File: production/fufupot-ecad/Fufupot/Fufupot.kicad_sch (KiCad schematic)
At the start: 56 parts, among them IC1 FOD3150, J1 Conn_01x04_Pin, J1 USB_B, J10 Conn_01x03, J3 Conn_01x03, J4 Conn_01x02_Pin, J5 Conn_01x02_Pin, J6 Conn_01x03_Pin, J7 Conn_01x02_Pin, J9 Conn_01x04_Pin, SW1 SW_Push, U1 STGP8NC60KD, U2 FT232RL, U2 LM5165DRC, U3 USBLC6-2SC6, U4 ATMEGA328P-PN

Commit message: Update Fufupot.kicad_sch
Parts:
- removed J1, J9: Conn_01x04_Pin, symbol Connector:Conn_01x04_Pin
- removed J4, J5, J7: Conn_01x02_Pin, symbol Connector:Conn_01x02_Pin
- removed J6: Conn_01x03_Pin, symbol Connector:Conn_01x03_Pin
- added J1, J8: Conn_01x04, symbol Connector_Generic:Conn_01x04
- added J11: Conn_01x03, symbol Connector_Generic:Conn_01x03
- added J5, J6, J7: Conn_01x02, symbol Connector_Generic:Conn_01x02
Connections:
- net +48V: now also J10.3 (Pin_3)
- net +5V: now also J10.2 (Pin_2), J11.2 (Pin_2)
- net A4: now also J5.2 (Pin_2)
- net A5: now also J5.1 (Pin_1)
- net D_Buzz: now also J6.1 (Pin_1)
- net D_Red: now also J8.3 (Pin_3)
- net D_Switch: now also J8.2 (Pin_2)
- net GND: now also J10.1 (Pin_1), J11.3 (Pin_3), J6.2 (Pin_2), J7.2 (Pin_2), J8.1 (Pin_1), J8.4 (Pin_4); no longer U2.18 (GND), U2.21 (GND), U2.7 (GND)
- net MISO: now also J1.3 (Pin_3)
- net MOSI: now also J1.2 (Pin_2)
- net SCK: now also J1.4 (Pin_4)
- net SS: now also J1.1 (Pin_1)
- net at R2.2: now also J11.1 (Pin_1)
- net at R2.2: now also J7.1 (Pin_1)
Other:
- moved on the sheet: C1, C3, C4, C5, IC1, J3, L1, L2, R1, R19, R2, R3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

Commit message: Kicad updates yay
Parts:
- removed 102PS1J1, 102PS1J2: 1k, symbol Device:R
- removed L1: L, symbol Device:L
- added J12, J4, J9: Conn_01x02, B2B-XH-A_LF__SN_:JST_B2B-XH-A_LF__SN_, symbol Connector_Generic:Conn_01x02
- C3: footprint (none) -> U1-E_NCH; symbol Device:C_Polarized -> 2023-11-09_20-43-14:UVZ1E100MDD
- C4: footprint (none) -> 8600footprint:CAP_WCAP-ATG5_05.0X11.0_WRE; symbol Device:C_Polarized -> 2023-11-09_20-51-41:860020772001
- C5: footprint (none) -> ECWfootprints:CAP_ECWFL_STRAIGHT_20.5LX11.9TX18.5H_PAN; symbol Device:C_Polarized -> 2023-11-09_20-58-51:ECW-F6364JL
- IC1: footprint DIP762W56P254L966H508Q8N -> FODfootprints:SMD8_9P91X6P86_ONS
- J1, J8: footprint (none) -> 4PINfootprints:CONN_B4B-XH-A_JST
- J10, J11, J3: footprint (none) -> 3PINfootprints:CONN_B3B-ZR_JST
- J5, J6, J7: footprint (none) -> B2B-XH-A_LF__SN_:JST_B2B-XH-A_LF__SN_
- L2: footprint (none) -> INDPM:INDPM176169X700N; symbol Device:L -> SRP1770CC-100M:SRP1770CC-100M; Height (none) -> 7; Manufacturer_Name (none) -> Bourns; Manufacturer_Part_Number (none) -> SRP1770CC-100M
- R1: footprint (none) -> SQPfootprints:RES_SQP500_22X9P5_YAG; symbol Device:R -> 2023-11-09_21-42-51:SQP500JB-0R91
- R12, R13, R19, R2, R20, R3, R4, R5, R7: footprint (none) -> Resistor_SMD:R_0805_2012Metric
- R2: value 220 -> 200; footprint (none) -> Resistor_SMD:R_0805_2012Metric
- U1: footprint TO-220FP_STM -> TO225P1040X460X1968-3(1):TO225P1040X460X1968-3
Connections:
- net +5V: now also J12.2 (Pin_2), J9.2 (Pin_2)
- net A2: now also J9.1 (Pin_1)
- net A3: now also J12.1 (Pin_1)
- net GND: now also C1.2
- net at C5.2, U1.2 (C): now also J4.1 (Pin_1)
- net at C1.1, C5.1, L2.2: now also J4.2 (Pin_2)

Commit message: Fixed switches
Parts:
- 16MHz1: footprint 16 MHz Xtal Osc:XTAL_ABL-16_ABR -> crystalfootprints:XTAL_ABL-16_ABR
- C5, C6: footprint 22 pF Cap:CAP_K-SERIES_15-L2_VIS -> 22pFfootprints:CAP_K-SERIES_15-L2_VIS
- C7: footprint 10 uF Cap:CAP_YX_5X11_RUB -> 10uFfootprints:CAP_YX_5X11_RUB
- C8: footprint (none) -> 0.1uFfootprints:CAP_Y5VE5TL2_VIS
- SW1: footprint (none) -> TS02-66-50-BK-100-SCR-D:SW_TS02-66-50-BK-100-SCR-D
- SW1: footprint Button_Switch_SMD:SW_DIP_SPSTx04_Slide_6.7x11.72mm_W6.73mm_P2.54mm_LowProfile_JPin -> TS02-66-50-BK-100-SCR-D:SW_TS02-66-50-BK-100-SCR-D
- U4: footprint footprints:28P3_ATM -> ATmegafootprints:28P3_ATM
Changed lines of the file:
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@@
       (effects (font (size 1.27 1.27)) (justify left))
     )
-    (property "Footprint" "22 pF Cap:CAP_K-SERIES_15-L2_VIS" (at 281.94 235.2548 0)
+    (property "Footprint" "22pFfootprints:CAP_K-SERIES_15-L2_VIS" (at 281.94 235.2548 0)
       (effects (font (size 1.27 1.27)) hide)
     )
@@
       (effects (font (size 1.27 1.27)))
     )
-    (property "Footprint" "" (at 172.72 115.57 0)
+    (property "Footprint" "TS02-66-50-BK-100-SCR-D:SW_TS02-66-50-BK-100-SCR-D" (at 172.72 115.57 0)
       (effects (font (size 1.27 1.27)) hide)
     )
@@
       (effects (font (size 1.27 1.27)) (justify left))
     )
-    (property "Footprint" "22 pF Cap:CAP_K-SERIES_15-L2_VIS" (at 281.94 221.2848 0)
+    (property "Footprint" "22pFfootprints:CAP_K-SERIES_15-L2_VIS" (at 281.94 221.2848 0)
       (effects (font (size 1.27 1.27)) hide)
     )
@@
       (effects (font (size 1.27 1.27)) (justify left))
     )
-    (property "Footprint" "" (at 289.2552 205.74 0)
+    (property "Footprint" "0.1uFfootprints:CAP_Y5VE5TL2_VIS" (at 289.2552 205.74 0)
       (effects (font (size 1.27 1.27)) hide)
     )
@@
       (effects (font (size 1.524 1.524)))
     )
-    (property "Footprint" "footprints:28P3_ATM" (at 288.29 199.39 0)
+    (property "Footprint" "ATmegafootprints:28P3_ATM" (at 288.29 199.39 0)
       (effects (font (size 1.27 1.27) italic) hide)
     )
@@
       (effects (font (size 1.27 1.27)))
     )
-    (property "Footprint" "Button_Switch_SMD:SW_DIP_SPSTx04_Slide_6.7x11.72mm_W6.73mm_P2.54mm_LowProfile_JPin" (at 194.31 262.89 0)
+    (property "Footprint" "TS02-66-50-BK-100-SCR-D:SW_TS02-66-50-BK-100-SCR-D" (at 194.31 262.89 0)
       (effects (font (size 1.27 1.27)) hide)
     )
@@
       (effects (font (size 1.27 1.27)) (justify right))
     )
-    (property "Footprint" "16 MHz Xtal Osc:XTAL_ABL-16_ABR" (at 287.02 228.6 0)
+    (property "Footprint" "crystalfootprints:XTAL_ABL-16_ABR" (at 287.02 228.6 0)
       (effects (font (size 1.27 1.27)) hide)
     )
@@
       (effects (font (size 1.27 1.27)) (justify left))
     )
-    (property "Footprint" "10 uF Cap:CAP_YX_5X11_RUB" (at 282.9052 205.74 0)
-      (effects (font (size 1.27 1.27)) hide)
-    )
+    (property "Footprint" "10uFfootprints:CAP_YX_5X11_RUB" (at 282.9052 205.74 0)
+      (effects (font (size 1.27 1.27)) hide)
+    )

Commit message: Updating USB
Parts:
- J1: footprint Connector_USB:USB_Micro-B_Amphenol_10104110_Horizontal -> UJ2-BH-W1-TH:CUI_UJ2-BH-W1-TH
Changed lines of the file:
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@@
       (effects (font (size 1.27 1.27)))
     )
-    (property "Footprint" "Connector_USB:USB_Micro-B_Amphenol_10104110_Horizontal" (at 31.75 114.3 0)
+    (property "Footprint" "UJ2-BH-W1-TH:CUI_UJ2-BH-W1-TH" (at 31.75 114.3 0)
       (effects (font (size 1.27 1.27)) hide)
     )

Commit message: pcb layout
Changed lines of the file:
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@@
   (junction (at 322.58 113.03) (diameter 0) (color 0 0 0 0)
   )
-  (junction (at 175.26 241.3) (diameter 0) (color 0 0 0 0)
-  )
   (junction (at 370.84 57.15) (diameter 0) (color 0 0 0 0)
   )
@@
   )
   (junction (at 271.78 46.99) (diameter 0) (color 0 0 0 0)
-  )
-  (junction (at 175.26 238.76) (diameter 0) (color 0 0 0 0)
-  )
-  (junction (at 175.26 245.11) (diameter 0) (color 0 0 0 0)
   )
   (junction (at 49.53 48.26) (diameter 0) (color 0 0 0 0)
@@
     (stroke (width 0) (type default))
   )
-  (wire (pts (xy 175.26 238.76) (xy 184.15 238.76))
-    (stroke (width 0) (type default))
-  )
   (wire (pts (xy 26.67 191.77) (xy 35.56 191.77))
     (stroke (width 0) (type default))
@@
     (stroke (width 0) (type default))
   )
-  (wire (pts (xy 175.26 236.22) (xy 175.26 238.76))
-    (stroke (width 0) (type default))
-  )
   (wire (pts (xy 364.49 76.2) (xy 361.95 76.2))
     (stroke (width 0) (type default))
@@
     (stroke (width 0) (type default))
   )
-  (wire (pts (xy 184.15 236.22) (xy 175.26 236.22))
+  (wire (pts (xy 176.53 236.22) (xy 176.53 237.49))
     (stroke (width 0) (type default))
   )
@@
     (stroke (width 0) (type default))
   )
-  (wire (pts (xy 175.26 241.3) (xy 184.15 241.3))
-    (stroke (width 0) (type default))
-  )
   (wire (pts (xy 341.63 62.23) (xy 344.17 62.23))
     (stroke (width 0) (type default))
@@
     (stroke (width 0) (type default))
   )
-  (wire (pts (xy 175.26 241.3) (xy 175.26 245.11))
-    (stroke (width 0) (type default))
-  )
   (wire (pts (xy 322.58 113.03) (xy 323.85 113.03))
     (stroke (width 0) (type default))
@@
   )
   (wire (pts (xy 360.68 237.49) (xy 367.03 237.49))
-    (stroke (width 0) (type default))
-  )
-  (wire (pts (xy 175.26 238.76) (xy 175.26 241.3))
     (stroke (width 0) (type default))
   )
@@
         )
       )
+    )
+  )
+  (symbol (lib_id "power:GND") (at 176.53 237.49 0) (unit 1)
+    (in_bom yes) (on_board yes) (dnp no) (fields_autoplaced)
+    (property "Reference" "#PWR047" (at 176.53 243.84 0)
+      (effects (font (size 1.27 1.27)) hide)
+    )
+    (property "Value" "GND" (at 176.53 242.57 0)
+      (effects (font (size 1.27 1.27)))
+    )
+    (property "Footprint" "" (at 176.53 237.49 0)
+      (effects (font (size 1.27 1.27)) hide)
+    )
+    (property "Datasheet" "" (at 176.53 237.49 0)
+      (effects (font (size 1.27 1.27)) hide)
+    )
+    (pin "1")
+    (instances
+      (project "Fufupot"
+        (path "/e8bc21b1-eda8-45a8-be25-55b90339183f"
+          (reference "#PWR047") (unit 1)
+        )
+      )

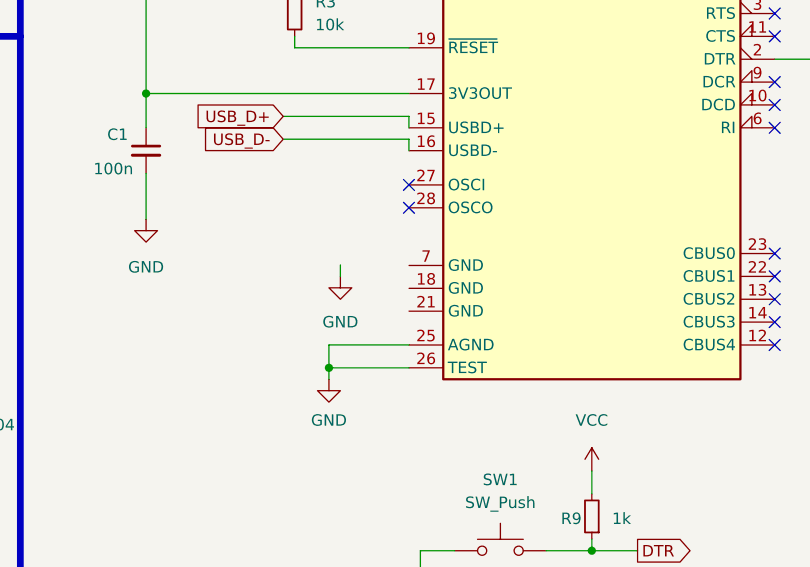
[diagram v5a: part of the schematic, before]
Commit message: fixed gnd of usb
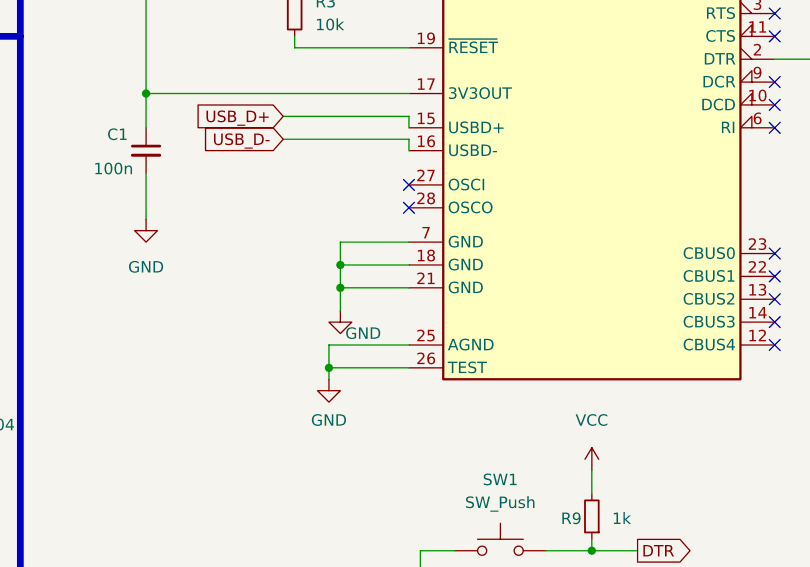
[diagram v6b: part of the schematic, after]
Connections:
- net GND: now also U2.18 (GND), U2.21 (GND), U2.7 (GND)
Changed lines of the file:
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@@
   (junction (at 171.45 203.2) (diameter 0) (color 0 0 0 0)
+  )
+  (junction (at 176.53 238.76) (diameter 0) (color 0 0 0 0)
+  )
+  (junction (at 176.53 236.22) (diameter 0) (color 0 0 0 0)
   )
   (junction (at 346.71 134.62) (diameter 0) (color 0 0 0 0)
@@
     (stroke (width 0) (type default))
   )
-  (wire (pts (xy 176.53 236.22) (xy 176.53 237.49))
-    (stroke (width 0) (type default))
-  )
   (wire (pts (xy 288.29 210.82) (xy 304.8 210.82))
     (stroke (width 0) (type default))
@@
     (stroke (width 0) (type default))
   )
+  (wire (pts (xy 176.53 238.76) (xy 184.15 238.76))
+    (stroke (width 0) (type default))
+  )
   (wire (pts (xy 273.05 54.61) (xy 273.05 57.15))
     (stroke (width 0) (type default))
@@
   )
   (wire (pts (xy 247.65 203.2) (xy 252.73 203.2))
+    (stroke (width 0) (type default))
+  )
+  (wire (pts (xy 176.53 236.22) (xy 176.53 238.76))
     (stroke (width 0) (type default))
   )
@@
     (stroke (width 0) (type default))
   )
+  (wire (pts (xy 176.53 233.68) (xy 176.53 236.22))
+    (stroke (width 0) (type default))
+  )
   (wire (pts (xy 360.68 201.93) (xy 367.03 201.93))
     (stroke (width 0) (type default))
@@
   )
   (wire (pts (xy 360.68 219.71) (xy 367.03 219.71))
+    (stroke (width 0) (type default))
+  )
+  (wire (pts (xy 176.53 236.22) (xy 184.15 236.22))
     (stroke (width 0) (type default))
   )
@@
     (stroke (width 0) (type default))
   )
+  (wire (pts (xy 184.15 233.68) (xy 176.53 233.68))
+    (stroke (width 0) (type default))
+  )
   (wire (pts (xy 175.26 245.11) (xy 184.15 245.11))
     (stroke (width 0) (type default))
@@
   )
   (wire (pts (xy 148.59 48.26) (xy 153.67 48.26))
+    (stroke (width 0) (type default))
+  )
+  (wire (pts (xy 176.53 238.76) (xy 176.53 241.3))
     (stroke (width 0) (type default))
   )
@@
     )
   )
-  (symbol (lib_id "power:GND") (at 176.53 237.49 0) (unit 1)
-    (in_bom yes) (on_board yes) (dnp no) (fields_autoplaced)
-    (property "Reference" "#PWR047" (at 176.53 243.84 0)
-      (effects (font (size 1.27 1.27)) hide)
-    )
-    (property "Value" "GND" (at 176.53 242.57 0)
-      (effects (font (size 1.27 1.27)))
-    )
-    (property "Footprint" "" (at 176.53 237.49 0)
-      (effects (font (size 1.27 1.27)) hide)
-    )
-    (property "Datasheet" "" (at 176.53 237.49 0)
-      (effects (font (size 1.27 1.27)) hide)
-    )
+  (symbol (lib_id "power:GND") (at 176.53 241.3 0) (unit 1)
+    (in_bom yes) (on_board yes) (dnp no)
+    (property "Reference" "#PWR047" (at 176.53 247.65 0)
+      (effects (font (size 1.27 1.27)) hide)
+    )
+    (property "Value" "GND" (at 179.07 243.84 0)
+      (effects (font (size 1.27 1.27)))
+    )
+    (property "Footprint" "" (at 176.53 241.3 0)
+      (effects (font (size 1.27 1.27)) hide)
+    )
+    (property "Datasheet" "" (at 176.53 241.3 0)
+      (effects (font (size 1.27 1.27)) hide)
+    )

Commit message: Final Draft, Need to be checked by Andy
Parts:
- removed J5: Conn_01x02, B2B-XH-A_LF__SN_:JST_B2B-XH-A_LF__SN_, symbol Connector_Generic:Conn_01x02
- added J13: Conn_01x03, pcbmount3footprints:282837-3_TYC, symbol Connector_Generic:Conn_01x03
- J1, J8: footprint 4PINfootprints:CONN_B4B-XH-A_JST -> pcbmount4footprints:282837-4_TYC
- J10, J11, J3: footprint 3PINfootprints:CONN_B3B-ZR_JST -> pcbmount3footprints:282837-3_TYC
- J12, J6, J7, J9: footprint B2B-XH-A_LF__SN_:JST_B2B-XH-A_LF__SN_ -> KF301-2P:HANDSON_KF301-2P
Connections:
- net +15V is gone; now on net +16V: C3.1, IC1.8 (VDD)
- net VCC is gone; now on net +5V: R7.1, R9.2
- net A4: now also J13.1 (Pin_1)
- net A5: now also J13.2 (Pin_2)
- net PWM Speed Control: now also J13.3 (Pin_3)

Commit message: Actual Final Draft- No errors
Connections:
- net at C3.2, IC1.5 (VSS), R1.1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: no longer R3.1, R4.2, U1.1 (G)
- new net: R3.1, R4.2, U1.1 (G)
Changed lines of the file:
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@@
   (junction (at 165.1 62.23) (diameter 0) (color 0 0 0 0)
-  )
-  (junction (at 331.47 113.03) (diameter 0) (color 0 0 0 0)
   )
   (junction (at 190.5 120.65) (diameter 0) (color 0 0 0 0)
@@
     (stroke (width 0) (type default))
   )
-  (wire (pts (xy 331.47 100.33) (xy 331.47 113.03))
+  (wire (pts (xy 331.47 100.33) (xy 331.47 134.62))
     (stroke (width 0) (type default))
   )
@@
     (stroke (width 0) (type default))
   )
-  (wire (pts (xy 331.47 113.03) (xy 331.47 134.62))
-    (stroke (width 0) (type default))
-  )
